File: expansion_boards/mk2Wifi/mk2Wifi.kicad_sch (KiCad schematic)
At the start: 18 parts, among them J4 OLED, SW1 GPIO0, SW2 RESET, U1 ESP32-WROOM-32E, U2 AP2112R5-3.3TRG1

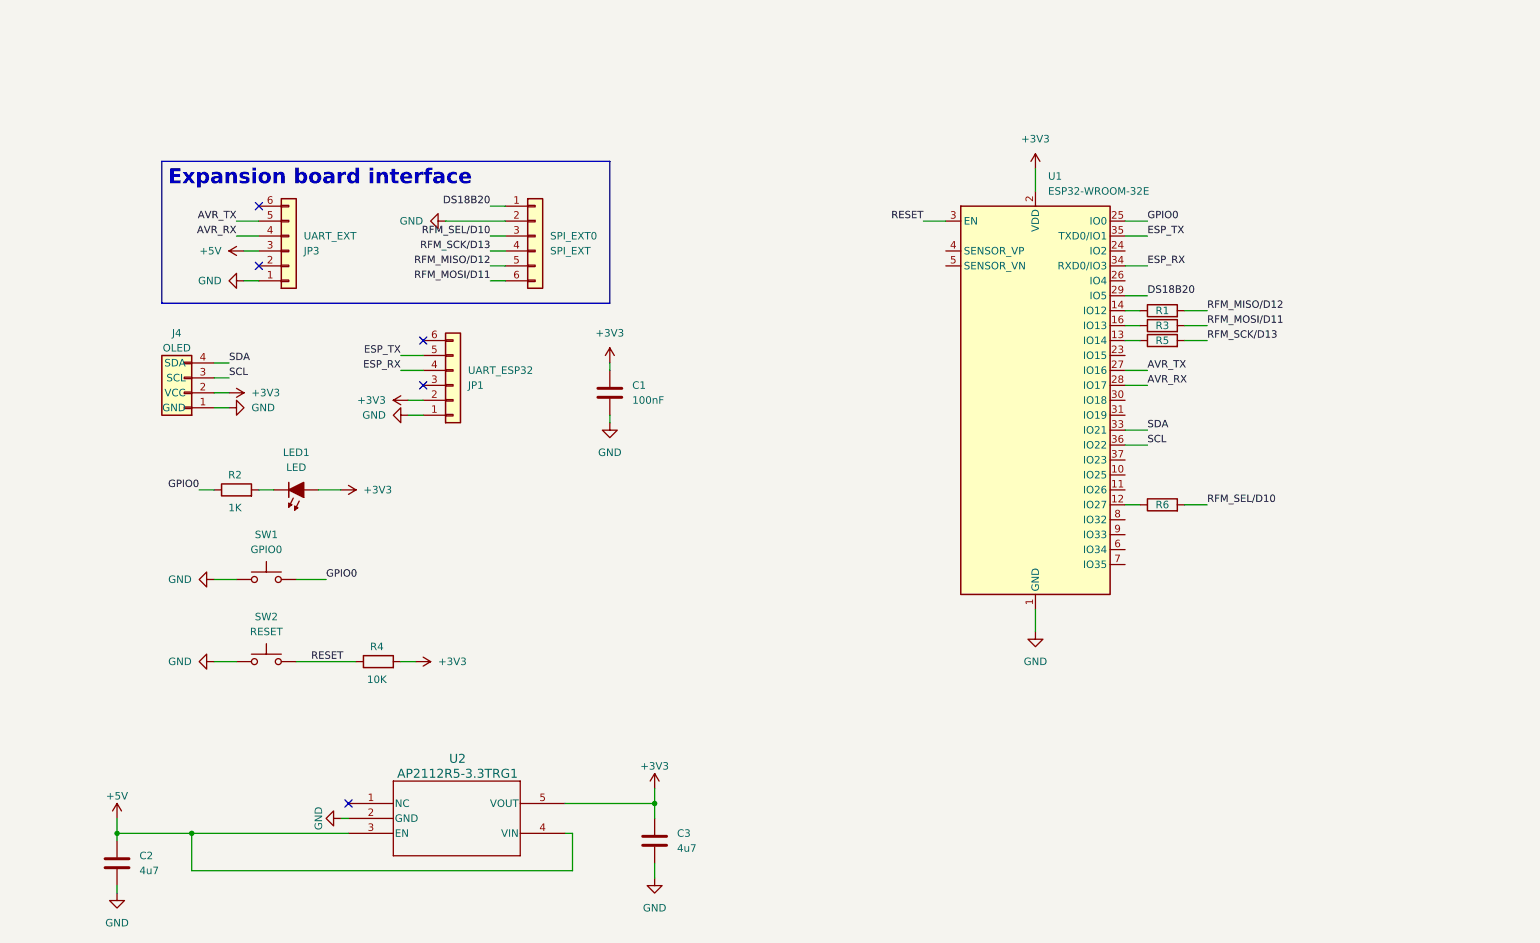
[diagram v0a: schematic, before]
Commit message: Swap mk2Wifi to ESP32-C3-MINI-1 with USB-C and SPI protection
Replace ESP32-WROOM-32 with ESP32-C3-MINI-1 (native USB, RISC-V).
Add USB-C connector (J2) with 5.1K CC pull-down resistors (R7, R8).
Add 1K series protection resistors on SPI outputs (R5/MOSI, R6/SCK,
R9/SEL). Remove JP1 UART header. Switch passives to 0402/0603.
Add local symbol and footprint libraries for ESP32-C3 and USB-C.

Co-Authored-By: Claude Opus 4.6 <noreply@anthropic.com>
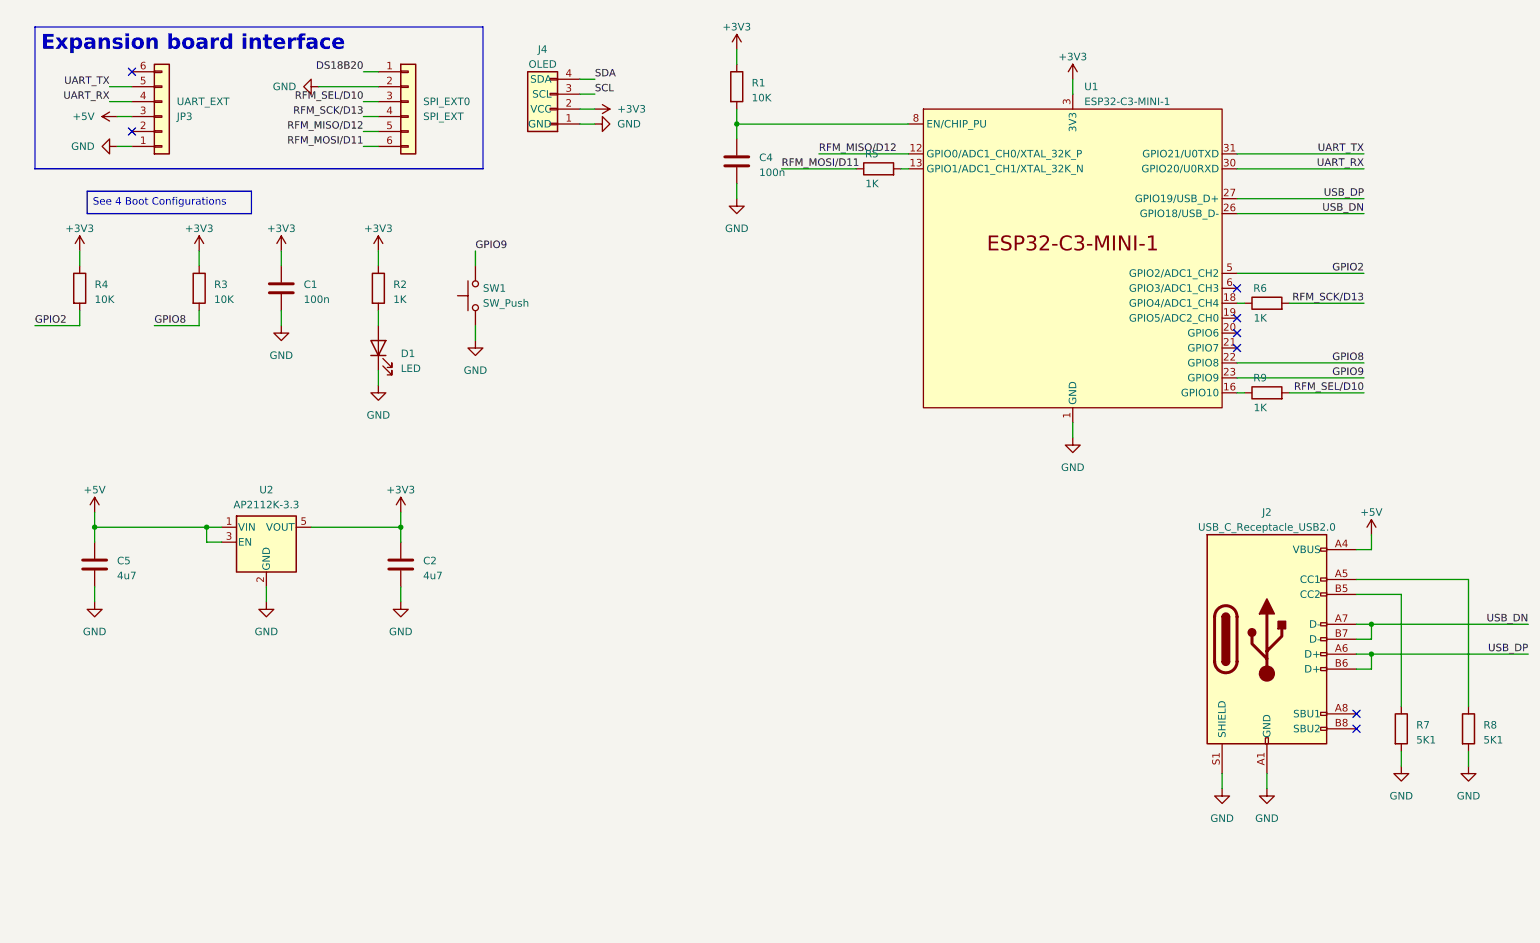
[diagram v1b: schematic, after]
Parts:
- removed C1: 100nF, PCM_Capacitor_SMD_Handsoldering_AKL:C_1206_3216Metric_Pad1.42x1.75mm, symbol PCM_Capacitor_AKL:C_Disc_D4.7mm_W2.5mm_P5.00mm
- removed C3: 4u7, PCM_Capacitor_SMD_Handsoldering_AKL:C_1206_3216Metric_Pad1.42x1.75mm, symbol Device:C
- removed JP1: UART_ESP32, Connector_PinSocket_2.54mm:PinSocket_1x06_P2.54mm_Vertical, symbol Connector_Generic:Conn_01x06
- removed LED1: LED, PCM_LED_SMD_Handsoldering_AKL:LED_1206_3216Metric_Pad1.42x1.75mm, symbol PCM_LED_AKL:LED_3mm
- removed SW2: RESET, Button_Switch_SMD:SW_SPST_CK_RS282G05A3, symbol Switch:SW_Push
- removed U1: ESP32-WROOM-32E, RF_Module:ESP32-WROOM-32D, symbol RF_Module:ESP32-WROOM-32E
- removed U2: AP2112R5-3.3TRG1, PCM_Package_TO_SOT_SMD_AKL:Diodes_SOT-89-5, symbol UserDef:AP2112R5-3.3TRG1
- added C1, C4: 100n, Capacitor_SMD:C_0402_1005Metric, symbol Device:C
- added C2: 4u7, Capacitor_SMD:C_0603_1608Metric, symbol Device:C
- added D1: LED, LED_SMD:LED_0603_1608Metric, symbol Device:LED
- added J2: USB_C_Receptacle_USB2.0, valcon-usb:CSP-USC16-TR, symbol Connector:USB_C_Receptacle_USB2.0
- added R7, R8: 5K1, Resistor_SMD:R_0402_1005Metric, symbol Device:R
- added R9: 1K, Resistor_SMD:R_0402_1005Metric, symbol Device:R
- added U1: ESP32-C3-MINI-1, PCM_Espressif:ESP32-C3-MINI-1, symbol PCM_Espressif:ESP32-C3-MINI-1
- added U2: AP2112K-3.3, Package_TO_SOT_SMD:SOT-23-5, symbol Regulator_Linear:AP2112K-3.3
- C5: renamed from C2; footprint PCM_Capacitor_SMD_Handsoldering_AKL:C_1206_3216Metric_Pad1.42x1.75mm -> Capacitor_SMD:C_0603_1608Metric
- R1, R3: value 1K -> 10K; footprint PCM_Resistor_SMD_AKL:R_1206_3216Metric_Pad1.42x1.75mm_HandSolder -> Resistor_SMD:R_0402_1005Metric; LCSC PN (none) -> C25744; Option X -> (none)
- R2: footprint PCM_Resistor_SMD_AKL:R_1206_3216Metric_Pad1.42x1.75mm_HandSolder -> Resistor_SMD:R_0402_1005Metric; LCSC PN (none) -> C11702; Option X -> (none)
- R4: footprint PCM_Resistor_SMD_AKL:R_1206_3216Metric_Pad1.42x1.75mm_HandSolder -> Resistor_SMD:R_0402_1005Metric; LCSC PN (none) -> C25744; Option X -> (none)
- R5, R6: footprint PCM_Resistor_SMD_AKL:R_1206_3216Metric_Pad1.42x1.75mm_HandSolder -> Resistor_SMD:R_0402_1005Metric; Option X -> (none)
- SW1: value GPIO0 -> SW_Push; footprint Button_Switch_SMD:SW_SPST_CK_RS282G05A3 -> Button_Switch_SMD:SW_Tactile_SPST_NO_Straight_CK_PTS636Sx25SMTRLFS; LCSC PN (none) -> C2689642
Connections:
- net RESET is gone; now on net +3V3: R4.1
- net +3V3: now also R1.1, R2.1, R3.1, C1.1, C2.1, U1.3 (3V3), U2.5 (VOUT); no longer R4.2
- net +5V: now also J2.A4 (VBUS), J2.A9 (VBUS), J2.B4 (VBUS), J2.B9 (VBUS), U2.1 (VIN), U2.3 (EN)
- net GND: now also C1.2, C2.2, C4.2, D1.1 (K), J2.A1 (GND), J2.A12 (GND), J2.B1 (GND), J2.B12 (GND), J2.S1 (SHIELD), R7.2, R8.2, U1.1 (GND), U1.11 (GND), U1.14 (GND), U1.2 (GND), U1.36 (GND), U1.37 (GND), U1.38 (GND), U1.39 (GND), U1.40 (GND), U1.41 (GND), U1.42 (GND), U1.43 (GND), U1.44 (GND), U1.45 (GND), U1.46 (GND), U1.47 (GND), U1.48 (GND), U1.49 (GND), U1.50 (GND), U1.51 (GND), U1.52 (GND), U1.53 (GND), U2.2 (GND)
- net RFM_MISO/D12: now also U1.12 (GPIO0/ADC1_CH0/XTAL_32K_P); no longer R1.2
- net RFM_MOSI/D11: now also R5.1; no longer R3.2
- net RFM_SCK/D13: now also R6.2; no longer R5.2
- net RFM_SEL/D10: now also R9.2; no longer R6.2
- net at R2.2: now also D1.2 (A)
- net at R6.1: now also U1.18 (GPIO4/ADC1_CH4)
- net AVR_RX renamed UART_RX
- net UART_RX: now also U1.30 (GPIO20/U0RXD)
- net AVR_TX renamed UART_TX
- net UART_TX: now also U1.31 (GPIO21/U0TXD)
- net GPIO0 renamed GPIO9
- net GPIO9: now also U1.23 (GPIO9); no longer R2.1
- new net: R9.1, U1.16 (GPIO10)
- new net: C4.1, R1.2, U1.8 (EN/CHIP_PU)
- new net: J2.A5 (CC1), R8.1
- new net: J2.B5 (CC2), R7.1
- new net: R5.2, U1.13 (GPIO1/ADC1_CH1/XTAL_32K_N)
- new net GPIO2: R4.2, U1.5 (GPIO2/ADC1_CH2)
- new net GPIO8: R3.2, U1.22 (GPIO8)
- new net USB_DN: J2.A7 (D-), J2.B7 (D-), U1.26 (GPIO18/USB_D-)
- new net USB_DP: J2.A6 (D+), J2.B6 (D+), U1.27 (GPIO19/USB_D+)
- no-connect marks 5 -> 8
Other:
- moved on the sheet: C5, J4, JP3, SPI_EXT0

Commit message: Update mk2Wifi headers to match mainboard refactoring
Rename SPI_EXT0 to TRIG_EXT0 with new pin labels (D5-D9) for home
automation triggers. Swap pin 1/2 (GND/D8). Move DS18B20 from
TRIG_EXT to UART_EXT pin 2. Update matching ESP32-side labels.

Co-Authored-By: Claude Opus 4.6 <noreply@anthropic.com>
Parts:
- TRIG_EXT0: renamed from SPI_EXT0; value SPI_EXT -> TRIG_EXT
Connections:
- net DS18B20: now also JP3.2 (Pin_2); no longer TRIG_EXT0.1 (Pin_1)
- net GND: now also TRIG_EXT0.1 (Pin_1); no longer TRIG_EXT0.2 (Pin_2)
- net RFM_MISO/D12 renamed D5
- net RFM_MOSI/D11 renamed D9
- net RFM_SCK/D13 renamed D6
- net RFM_SEL/D10 renamed D7
- new net D8: TRIG_EXT0.2 (Pin_2)
- no-connect marks 8 -> 7
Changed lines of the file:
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@@
 	)
 	(no_connect
-		(at 33.02 35.56)
-	)
-	(no_connect
 		(at 220.98 67.31)
 	)
@@
 	(wire
 		(pts
-			(xy 74.93 27.94) (xy 64.77 27.94)
+			(xy 74.93 27.94) (xy 72.39 27.94)
 		)
 		(stroke
@@
 		)
 	)
-	(label "RFM_MOSI{slash}D11"
+	(label "D9"
 		(at 72.39 38.1 180)
 		(effects
 			(font
-				(size 1.2446 1.2446)
+				(size 1.27 1.27)
 			)
 			(justify right bottom)
@@
 		)
 	)
-	(label "RFM_MISO{slash}D12"
+	(label "D5"
 		(at 149.86 39.37 0)
 		(effects
@@
 		)
 	)
-	(label "DS18B20"
-		(at 72.39 25.4 180)
-		(effects
-			(font
-				(size 1.27 1.27)
+	(symbol
+		(lib_id "power:GND")
+		(at 72.39 25.4 270)
+		(unit 1)
+		(exclude_from_sim no)
+		(in_bom yes)
+		(on_board yes)
+		(dnp no)
+		(fields_autoplaced yes)
+		(property "Reference" "#PWR030"
+			(at 66.04 25.4 0)
+			(effects
+				(font
+					(size 1.27 1.27)
+				)
+				(hide yes)
+			)
+		)
+		(property "Value" "GND"
+			(at 68.58 25.3999 90)
+			(effects
+				(font
+					(size 1.27 1.27)
+				)
+				(justify right)
+			)
+		)
+		(property "Footprint" ""
+			(at 72.39 25.4 0)
+			(effects
+				(font
+					(size 1.27 1.27)
+				)
+				(hide yes)
+			)
+		)
+		(property "Datasheet" ""
+			(at 72.39 25.4 0)
+			(effects
+				(font
+					(size 1.27 1.27)
+				)
+				(hide yes)
+			)
+		)
+		(property "Description" ""
+			(at 72.39 25.4 0)
+			(effects
+				(font
+					(size 1.27 1.27)
+				)
+			)
+		)
+		(pin "1"
+		)
+		(instances
+			(project "mk2Wifi"
+				(path "/8f85e568-8005-4933-a5bc-4fca9da3c7b3"
+					(reference "#PWR030")
+					(unit 1)
+				)
 			)
-			(justify right bottom)
 		)
 	)
-	(label "RFM_MISO{slash}D12"
+	(label "D5"
 		(at 72.39 35.56 180)
 		(effects
 			(font
-				(size 1.2446 1.2446)
+				(size 1.27 1.27)
 			)
 			(justify right bottom)
@@
 		)
 	)
-	(label "RFM_MOSI{slash}D11"
+	(label "D9"
 		(at 143.51 41.91 0)
 		(effects
@@
 		)
 	)
-	(label "RFM_SCK{slash}D13"
+	(label "D6"
 		(at 242.57 64.77 180)
 		(effects
@@
 		)
 	)
-	(label "RFM_SEL{slash}D10"
+	(label "D7"
 		(at 242.57 80.01 180)
 		(effects
@@
 		)
 	)
-	(label "RFM_SCK{slash}D13"
+	(label "D6"
 		(at 72.39 33.02 180)
 		(effects
 			(font
-				(size 1.2446 1.2446)
+				(size 1.27 1.27)
 			)
 			(justify right bottom)
 		)
 	)
-	(label "RFM_SEL{slash}D10"
+	(label "D7"
 		(at 72.39 30.48 180)
 		(effects
 			(font
-				(size 1.2446 1.2446)
+				(size 1.27 1.27)
 			)
 			(justify right bottom)
@@
 		(dnp no)
 		(fields_autoplaced yes)
-		(property "Reference" "SPI_EXT0"
+		(property "Reference" "TRIG_EXT0"
 			(at 82.55 30.4799 0)
 			(effects
@@
 			)
 		)
-		(property "Value" "SPI_EXT"
+		(property "Value" "TRIG_EXT"
 			(at 82.55 33.0199 0)
 			(effects
@@
 			(project "ESP32"
 				(path "/8f85e568-8005-4933-a5bc-4fca9da3c7b3"
-					(reference "SPI_EXT0")
+					(reference "TRIG_EXT0")
 					(unit 1)
 				)
@@
 		)
 	)
-	(symbol
-		(lib_id "power:GND")
-		(at 64.77 27.94 270)
-		(unit 1)
-		(exclude_from_sim no)
-		(in_bom yes)
-		(on_board yes)
-		(dnp no)
-		(fields_autoplaced yes)
-		(property "Reference" "#PWR013"
-			(at 58.42 27.94 0)
-			(effects
-				(font
-					(size 1.27 1.27)
-				)
-				(hide yes)
-			)
-		)
-		(property "Value" "GND"
-			(at 60.96 27.9399 90)
-			(effects
-				(font
-					(size 1.27 1.27)
-				)
-				(justify right)
-			)
-		)
-		(property "Footprint" ""
-			(at 64.77 27.94 0)
-			(effects
-				(font
-					(size 1.27 1.27)
-				)
-				(hide yes)
-			)
-		)
-		(property "Datasheet" ""
-			(at 64.77 27.94 0)
-			(effects
-				(font
-					(size 1.27 1.27)
-				)
-				(hide yes)
-			)
-		)
-		(property "Description" "Power symbol creates a global label with name \"GND\" , ground"
-			(at 64.77 27.94 0)
-			(effects
-				(font
-					(size 1.27 1.27)
-				)
-				(hide yes)
-			)
-		)
-		(pin "1"
-		)
-		(instances
-			(project "ESP32"
-				(path "/8f85e568-8005-4933-a5bc-4fca9da3c7b3"
-					(reference "#PWR013")
-					(unit 1)
-				)
+	(label "D8"
+		(at 72.39 27.94 180)
+		(effects
+			(font
+				(size 1.27 1.27)
 			)
+			(justify right bottom)
 		)
 	)
@@
 		)
 	)
+	(wire
+		(pts
+			(xy 30.48 35.56) (xy 33.02 35.56)
+		)
+		(stroke
+			(width 0)
+			(type default)
+		)
+	)
+	(label "DS18B20"
+		(at 30.48 35.56 180)
+		(effects
+			(font
+				(size 1.27 1.27)
+			)
+			(justify right bottom)
+		)
+	)
